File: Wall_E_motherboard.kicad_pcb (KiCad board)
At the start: 4 copper layers, 81.1 x 71.4 mm, 69 parts, among them J1 Conn_01x02, J8 Conn_01x06_Socket, J9 Conn_01x02_Socket, Q1 PMOS, SW1 SW_SPST, SW2 SW_SPST, SW3 SW_SPST, U1 LM1085-ADJ, U2 STM32F411RCTx, U3 DRV8838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

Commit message: Routing Updates
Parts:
- added ArmL1: Conn_01x03_Socket, Connector_PinHeader_2.54mm:PinHeader_1x03_P2.54mm_Vertical, F.Cu at (116.2, 105.9)
- added ArmR1: Conn_01x03_Socket, Connector_PinHeader_2.54mm:PinHeader_1x03_P2.54mm_Vertical, F.Cu at (175.8, 106.1)
- added Camera1: Conn_01x08_Socket, Connector_PinHeader_2.54mm:PinHeader_1x08_P2.54mm_Vertical, F.Cu at (175.8, 67.4)
- added H1: MountingHole, MountingHole:MountingHole_3.2mm_M3, F.Cu at (125.0, 77.2)
- added H2: MountingHole, MountingHole:MountingHole_3.2mm_M3, F.Cu at (175.8, 61.2)
- added H3: MountingHole, MountingHole:MountingHole_3.2mm_M3, F.Cu at (123.2, 123.2)
- added H4: MountingHole, MountingHole:MountingHole_3.2mm_M3, F.Cu at (170.8, 123.5)
- added HandL1: Conn_01x03_Socket, Connector_PinHeader_2.54mm:PinHeader_1x03_P2.54mm_Vertical, F.Cu at (116.2, 114.9)
- added HandR1: Conn_01x03_Socket, Connector_PinHeader_2.54mm:PinHeader_1x03_P2.54mm_Vertical, F.Cu at (175.8, 115.1)
- added LeftMotor1: Conn_01x06_Socket, Connector_PinHeader_2.54mm:PinHeader_1x06_P2.54mm_Vertical, F.Cu at (116.2, 89.2)
- added R16: 10, Resistor_SMD:R_0603_1608Metric, F.Cu at (223.5, 91.4)
- added R17: 10, Resistor_SMD:R_0603_1608Metric, F.Cu at (223.5, 94.2)
- added R18: 10k, Resistor_SMD:R_0603_1608Metric, F.Cu at (157.4, 97.7)
- added R19: 10k, Resistor_SMD:R_0603_1608Metric, F.Cu at (159.0, 98.0)
- added Range1: Conn_01x04_Socket, Connector_PinHeader_2.54mm:PinHeader_1x04_P2.54mm_Vertical, F.Cu at (138.0, 122.0)
- added RightMotor1: Conn_01x06_Socket, Connector_PinHeader_2.54mm:PinHeader_1x06_P2.54mm_Vertical, F.Cu at (175.8, 89.2)
- C11, C9: value 0.1u -> 22u; footprint Capacitor_SMD:C_0603_1608Metric -> Capacitor_THT:CP_Radial_D5.0mm_P2.00mm
- Q1: value PMOS -> SI4435FDY-T1-GE3; footprint Package_TO_SOT_THT:TO-220-3_Vertical -> Wall_E_footprints:SO-8_VIS
- SW3: footprint Button_Switch_THT:SW_PUSH_6mm -> Button_Switch_SMD:SW_SPST_PTS645
- Y1: footprint Crystal:Crystal_SMD_HC49-SD -> Crystal:Crystal_SMD_3225-4Pin_3.2x2.5mm
- Y2, Y3: footprint Crystal:Crystal_SMD_HC49-SD -> Crystal:Crystal_SMD_3215-2Pin_3.2x1.5mm
- moved C12 196.9 mm to (255.3, 73.9)
- moved C13 196.9 mm to (255.3, 76.4)
- moved C14 196.9 mm to (255.3, 78.9)
- moved C15 196.9 mm to (255.3, 81.4)
- moved U4 162.0 mm to (247.2, 73.2)
- moved U5 162.0 mm to (247.2, 76.9)
- moved C25 162.0 mm to (256.8, 97.9)
- moved C9 116.0 mm to (171.0, 97.3), turned to -90 degrees
- moved C8 112.8 mm to (168.0, 96.0), turned to -135 degrees
- moved U3 84.1 mm to (171.5, 94.2), turned to 180 degrees
- moved Y3 72.1 mm to (129.2, 100.2), turned to 180 degrees
- moved C10 71.6 mm to (124.0, 91.8), turned to 45 degrees
- moved C21 63.0 mm to (132.1, 99.9), turned to 90 degrees
- moved C11 61.4 mm to (121.0, 90.5), turned to 90 degrees
- moved R7 60.7 mm to (134.1, 106.0), turned to -90 degrees
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- renumbered J8 to STLink1, J9 to UART1
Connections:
- net Net-(U6-PS0) renamed IMU_PS0
- net Net-(U6-PS1) renamed IMU_PS1
- C11 pad 1: GND -> Vin
- C11 pad 2: Vin -> GND
- C21 pad 2: GND -> Net-(C21-Pad2)
- C22 pad 2: GND -> Net-(C21-Pad2)
- C9 pad 1: GND -> Vin
- C9 pad 2: Vin -> GND
- F1 pad 2: Net-(Q1-D) -> Net-(F1-Pad2)
- Q1 pad 1: Net-(Q1-D) -> Net-(F1-Pad2)
- Q1 pad 2: Net-(Q1-G) -> Net-(F1-Pad2)
- Q1 pad 3: Vin -> Net-(F1-Pad2)
- R9 pad 1: Net-(Q1-G) -> Net-(Q1-Pad4)
- U2 pad 1: 5V -> 3.3V
- U2 pad 14: unconnected-(U2-PA0-Pad14) -> ENCA_left
- U2 pad 15: unconnected-(U2-PA1-Pad15) -> Bat_ADC
- U2 pad 21: unconnected-(U2-PA5-Pad21) -> CAM_SCLK
- U2 pad 22: unconnected-(U2-PA6-Pad22) -> Echo
- U2 pad 23: unconnected-(U2-PA7-Pad23) -> Trig
- U2 pad 26: unconnected-(U2-PB0-Pad26) -> DIR_left
- U2 pad 27: unconnected-(U2-PB1-Pad27) -> DIR_right
- U2 pad 29: unconnected-(U2-PB10-Pad29) -> ENCB_left
- U2 pad 41: unconnected-(U2-PA8-Pad41) -> R_Arm_PWM
- U2 pad 42: unconnected-(U2-PA9-Pad42) -> L_Arm_PWM
- U2 pad 43: unconnected-(U2-PA10-Pad43) -> R_Hand_PWM
- U2 pad 44: unconnected-(U2-PA11-Pad44) -> L_Hand_PWM
- U2 pad 53: unconnected-(U2-PC12-Pad53) -> CAM_CS
- U2 pad 56: unconnected-(U2-PB4-Pad56) -> CAM_MISO
- U2 pad 57: unconnected-(U2-PB5-Pad57) -> CAM_MOSI
- U2 pad 58: unconnected-(U2-PB6-Pad58) -> I2C_SCL
- U2 pad 59: unconnected-(U2-PB7-Pad59) -> ENCA_right
- U2 pad 61: unconnected-(U2-PB8-Pad61) -> ENCB_right
- U2 pad 62: unconnected-(U2-PB9-Pad62) -> I2C_SDA
- U3 pad 6: PH_right -> DIR_right
- U6 pad 10: unconnected-(U6-BL_IND-Pad10) -> GND
- U6 pad 11: unconnected-(U6-~{RESET}-Pad11) -> IMU_NRST
- U6 pad 14: unconnected-(U6-INT-Pad14) -> IMU_INT
- U6 pad 18: unconnected-(U6-COM2-Pad18) -> GND
- U6 pad 19: unconnected-(U6-COM1-Pad19) -> I2C_SCL
- U6 pad 20: unconnected-(U6-COM0-Pad20) -> I2C_SDA
- U6 pad 4: unconnected-(U6-~{BOOT_LOAD_PIN}-Pad4) -> 3.3V
- U7 pad 6: PH_left -> DIR_left
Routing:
- net Vin: track 17.9 -> 98.7 mm, vias 0 -> 4
- net 5V: track 54.5 -> 1.21 mm, vias 2 -> 1
- net CAM_SCLK: track 0.00 -> 46.6 mm, vias 0 -> 2
- net I2C_SCL: track 0.00 -> 45.2 mm
- net I2C_SDA: track 0.00 -> 41.4 mm
- net LED: track 12.8 -> 50.6 mm
- net CAM_MISO: track 0.00 -> 33.6 mm
- net CAM_MOSI: track 0.00 -> 29.5 mm
- net ENCB_right: track 0.00 -> 29.2 mm
- net ENCA_right: track 0.00 -> 28.7 mm
- net CAM_CS: track 0.00 -> 27.2 mm
- net PC15: track 23.7 -> 6.47 mm
- net Net-(F1-Pad2): track 0.00 -> 14.0 mm
- net ST_SWO: track 34.3 -> 21.8 mm
- net PH1: track 20.2 -> 8.09 mm
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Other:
- board size 81.1 x 71.4 mm -> 69.4 x 71.4 mm
- board text added: "Battery"
- board text added: "E-Stop"
- board text added: "On SW"

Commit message: continued routing
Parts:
- removed C12, C13, C14, C15: 0.1u, Capacitor_SMD:C_0603_1608Metric
- removed R16, R17: 10, Resistor_SMD:R_0603_1608Metric
- removed U4, U5: DRV8838, Package_SON:WSON-8-1EP_2x2mm_P0.5mm_EP0.9x1.6mm
- added TP1: TestPoint_Small, TestPoint:TestPoint_Pad_D1.0mm, F.Cu at (122.7, 99.6)
- added TP2: TestPoint_Small, TestPoint:TestPoint_Pad_D1.0mm, F.Cu at (188.0, 102.0)
- moved C25 102.7 mm to (154.1, 95.6), turned to 90 degrees
- moved R7 4.17 mm to (138.1, 107.2), turned to 0 degrees
- moved STLink1 4.04 mm to (162.6, 119.1)
- moved UART1 4.04 mm to (146.1, 119.1)
- moved H4 3.91 mm to (169.0, 120.0)
- moved H3 3.69 mm to (125.0, 120.0)
- moved C21 3.51 mm to (135.3, 101.2)
- moved C22 3.51 mm to (129.6, 101.2)
- moved U6 3.51 mm to (133.5, 106.0)
- moved Y3 3.51 mm to (132.5, 101.5)
- moved C19 3.51 mm to (132.0, 109.1)
- moved R5 3.51 mm to (129.6, 109.1)
- moved C24 3.51 mm to (128.9, 105.3)
- moved C20 3.51 mm to (128.9, 103.6)
- moved R6 3.51 mm to (128.9, 106.8)
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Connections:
- U2 pad 25: unconnected-(U2-PC5-Pad25) -> SL_left
- U2 pad 28: unconnected-(U2-PB2-Pad28) -> SL_right
- U2 pad 41: R_Arm_PWM -> L_Arm_PWM
- U2 pad 42: L_Arm_PWM -> L_Hand_PWM
- U2 pad 44: L_Hand_PWM -> R_Arm_PWM
- U2 pad 50: unconnected-(U2-PA15-Pad50) -> EN_right
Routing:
- net 5V: track 1.21 -> 124.8 mm, vias 1 -> 9
- net Vin: track 98.7 -> 190.1 mm, vias 4 -> 8
- net L_Hand_PWM: track 0.00 -> 52.4 mm
- net L_Arm_PWM: track 0.00 -> 49.6 mm
- net ENCB_left: track 0.00 -> 43.1 mm
- net DIR_left: track 0.00 -> 42.4 mm
- net SL_left: track 0.00 -> 41.5 mm
- net ENCA_left: track 0.00 -> 33.5 mm, vias 0 -> 1
- net DIR_right: track 0.00 -> 29.4 mm
- net SL_right: track 0.00 -> 28.9 mm
- net R_Hand_PWM: track 0.00 -> 25.8 mm
- net Bat_ADC: track 1.61 -> 27.4 mm, vias 0 -> 2
- net I2C_SDA: track 41.4 -> 63.9 mm
- net I2C_SCL: track 45.2 -> 67.6 mm
- net R_Arm_PWM: track 0.00 -> 18.7 mm
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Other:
- board size 69.4 x 71.4 mm -> 69.4 x 67.8 mm

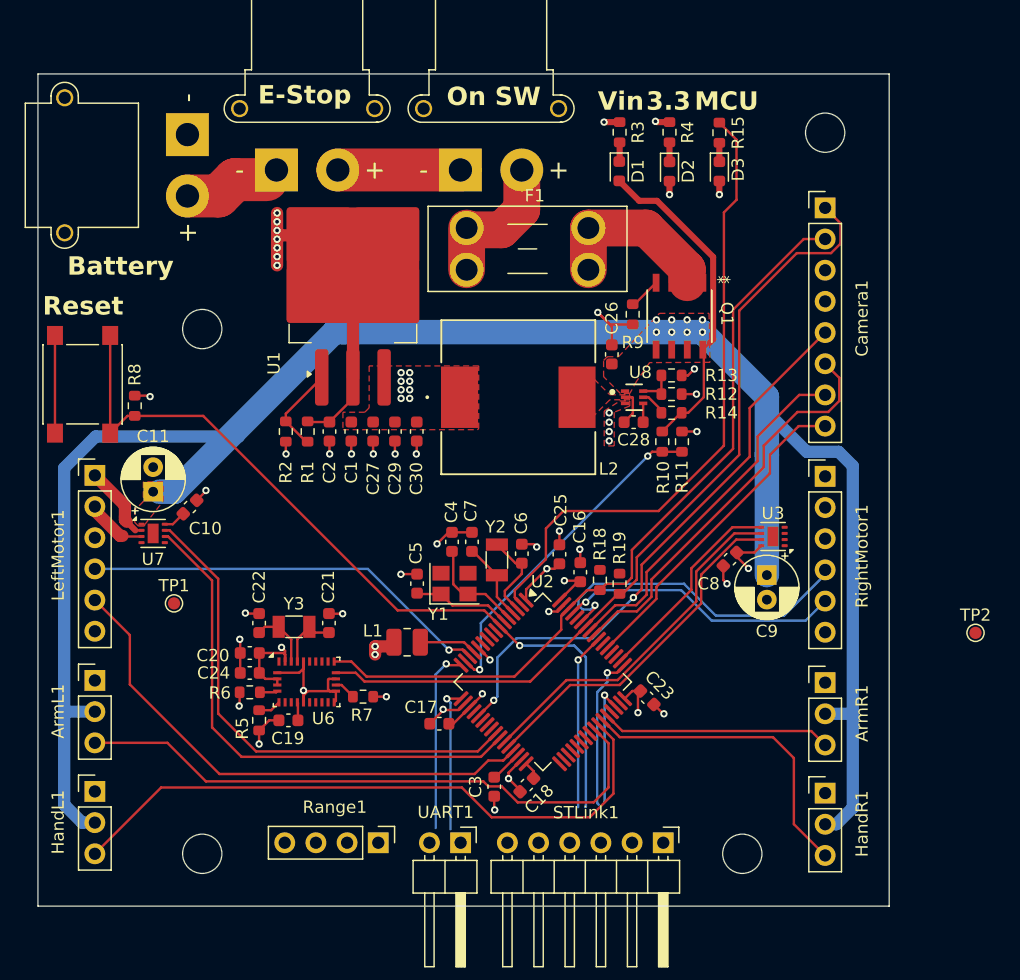
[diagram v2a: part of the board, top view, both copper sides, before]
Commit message: Routing first draft complete
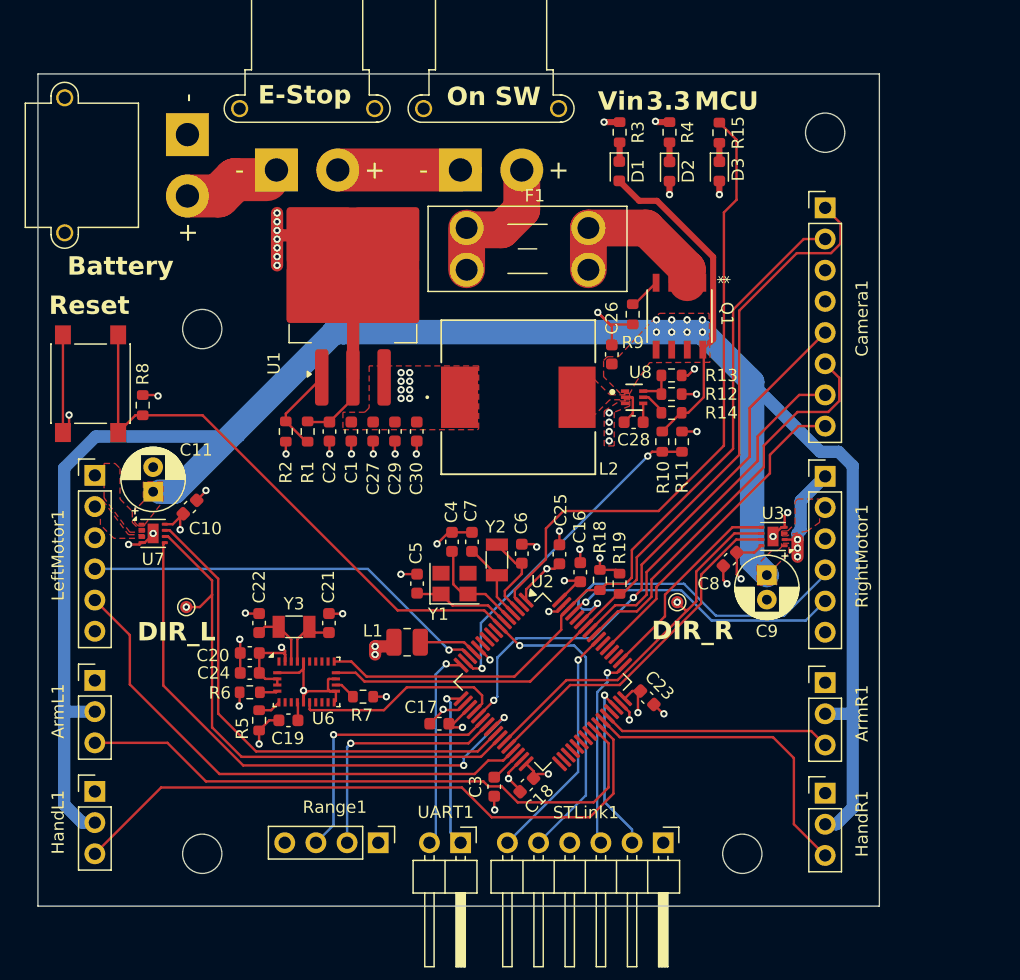
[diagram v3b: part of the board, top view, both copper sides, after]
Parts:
- moved TP2 24.4 mm to (163.7, 99.5)
- moved TP1 1.04 mm to (123.7, 99.9)
- moved R8 0.65 mm to (120.2, 83.5)
- moved SW3 0.65 mm to (115.9, 81.7)
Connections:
- net IMU_PS0 renamed Net-(U6-PS0)
- net IMU_PS1 renamed Net-(U6-PS1)
- C21 pad 2: Net-(C21-Pad2) -> GND
- C22 pad 2: Net-(C21-Pad2) -> GND
- U2 pad 20: unconnected-(U2-PA4-Pad20) -> IMU_NRST
- U2 pad 24: unconnected-(U2-PC4-Pad24) -> EN_left
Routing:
- net EN_left: track 0.00 -> 45.6 mm, vias 0 -> 2
- net Echo: track 0.00 -> 22.0 mm, vias 0 -> 1
- net Trig: track 0.00 -> 20.0 mm, vias 0 -> 1
- net IMU_NRST: track 0.00 -> 17.3 mm
- net GND: track 70.0 -> 80.6 mm, vias 35 -> 41
- net M1_right: track 0.00 -> 8.53 mm, vias 0 -> 3
- net M1_left: track 6.48 -> 0.00 mm
- net 3.3V: track 59.8 -> 65.5 mm, vias 18 -> 21
- net ST_SWO: track 14.4 -> 19.7 mm
- net M2_left: track 5.35 -> 0.68 mm
- net ST_SWDIO: track 10.1 -> 14.3 mm
- net NRST: track 67.7 -> 71.5 mm
- net ST_SWCLK: track 12.8 -> 16.0 mm
- net DIR_left: track 42.4 -> 44.9 mm, vias 0 -> 1
- net Net-(C21-Pad2): track 2.26 -> 0.00 mm
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- added copper zone on F.Cu, net M1_left
- added copper zone on F.Cu, net M2_left
- added copper zone on F.Cu, net M2_right
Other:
- board size 69.4 x 67.8 mm -> 68.6 x 67.8 mm
- board text added: "DIR_L"
- board text added: "DIR_R"

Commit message: Final commit before Charlie review
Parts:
- added TP3: TestPoint_Small, TestPoint:TestPoint_Pad_D1.0mm, F.Cu at (160.2, 90.6)
- C2, C27, C29: footprint Capacitor_SMD:C_0603_1608Metric -> Capacitor_THT:CP_Radial_D5.0mm_P2.00mm
- R1: value R -> 16.5k 1%
- R2: value R -> 10k 1%
- moved C2 14.7 mm to (129.8, 72.0), turned to 180 degrees
- moved R1 7.79 mm to (130.6, 78.4)
- moved C27 7.32 mm to (131.6, 85.6)
- moved R2 5.01 mm to (129.8, 81.0), turned to 180 degrees
- moved C1 3.66 mm to (140.8, 85.6)
- moved C29 3.50 mm to (137.2, 85.6)
- moved R8 1.33 mm to (121.5, 83.2)
- moved SW3 1.33 mm to (117.2, 81.4)
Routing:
- net 5V: track 124.8 -> 132.4 mm, vias 9 -> 1
- net /Power Regulation/buck_sw: track 2.93 -> 9.04 mm, vias 0 -> 1
- net GND: track 80.6 -> 77.4 mm, vias 41 -> 38
- net Net-(U1-ADJ): track 7.24 -> 6.00 mm
- net NRST: track 71.5 -> 70.3 mm
- net 3.3V: track 65.5 -> 65.9 mm, vias 21 -> 14
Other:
- board size 68.6 x 67.8 mm -> 68 x 68 mm
- board text added: "SW"

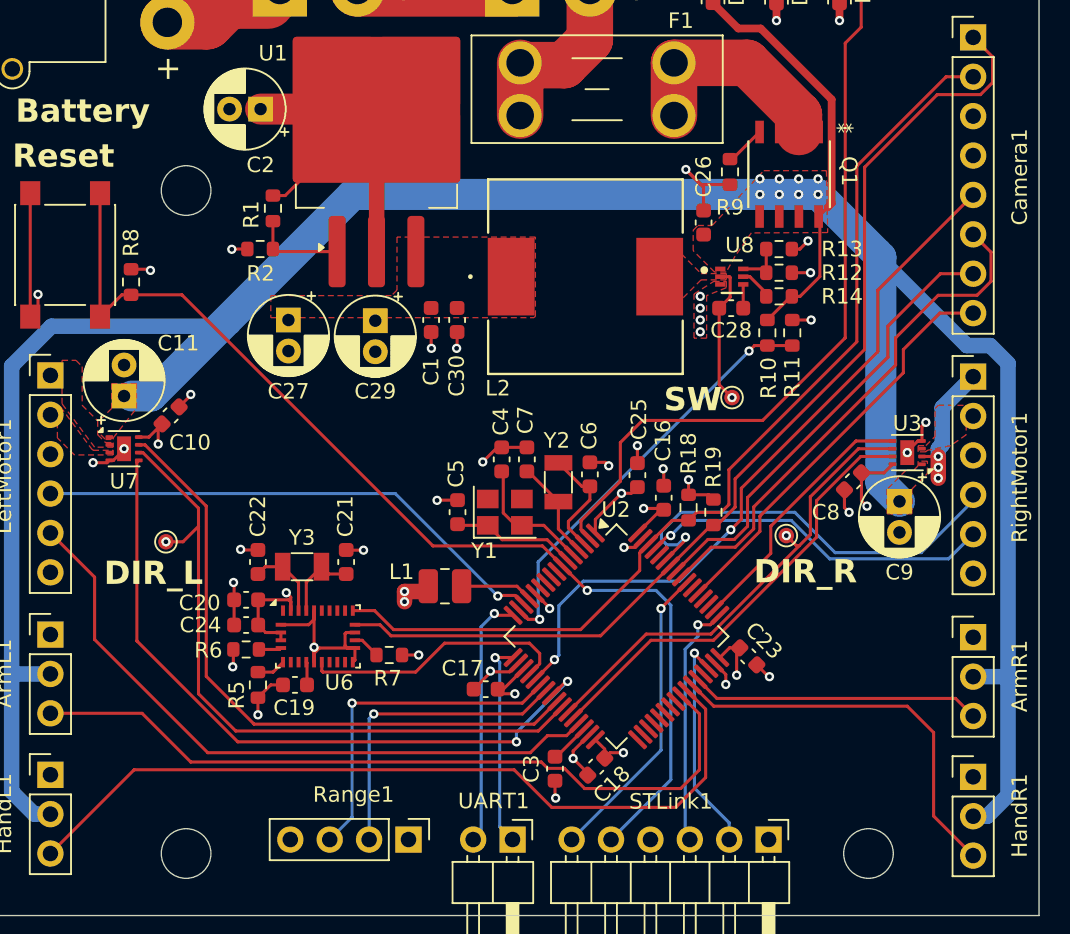
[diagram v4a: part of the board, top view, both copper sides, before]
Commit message: added resistor divider to Echo pin
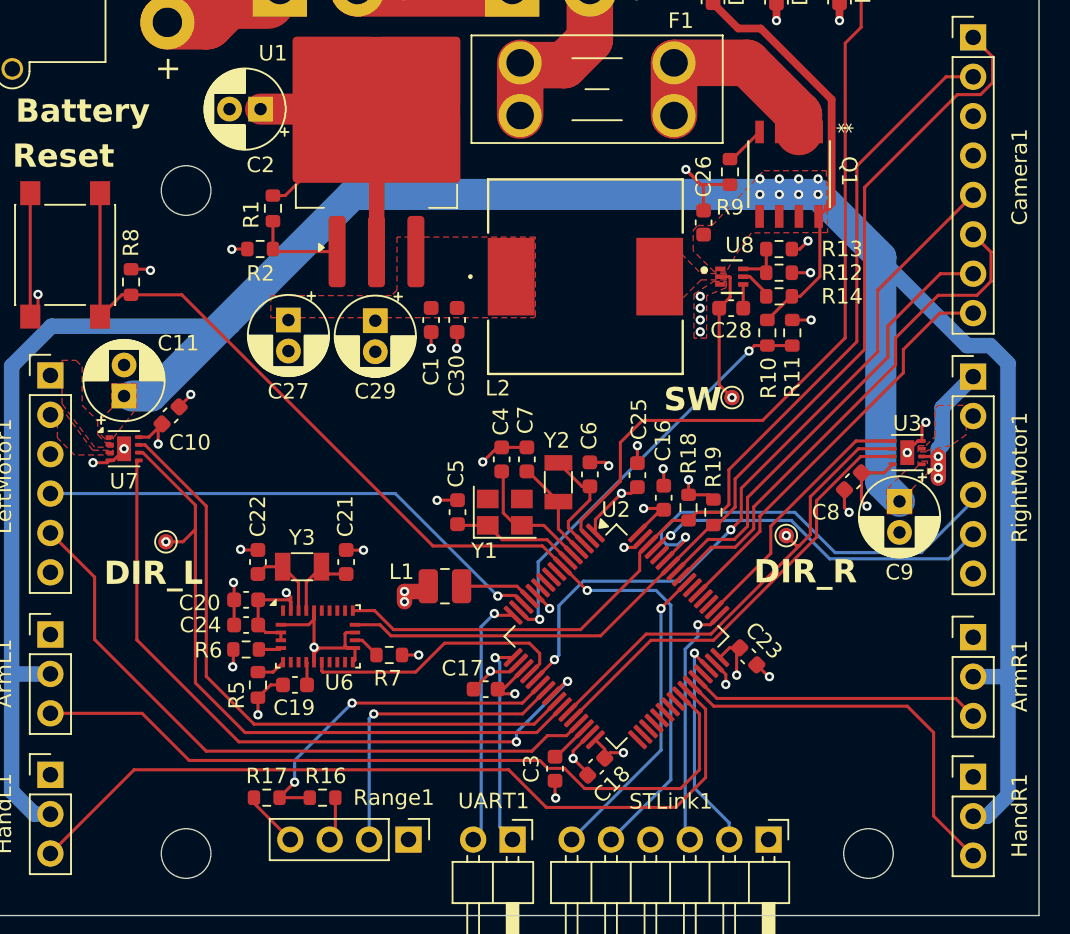
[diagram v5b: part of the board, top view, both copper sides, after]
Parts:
- added R16: 5k, Resistor_SMD:R_0603_1608Metric, F.Cu at (133.8, 116.4)
- added R17: 10k, Resistor_SMD:R_0603_1608Metric, F.Cu at (130.2, 116.4)
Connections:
- Range1 pad 3: Echo -> Net-(Range1-Pin_3)
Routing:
- net GND: track 77.4 -> 81.1 mm
- net Net-(Range1-Pin_3): track 0.00 -> 2.85 mm
- net I2C_SCL: track 67.6 -> 66.8 mm
- net Echo: track 22.0 -> 22.6 mm, vias 1 -> 2

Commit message: Final design before order
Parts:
- added C12: 0.1u, Capacitor_SMD:C_0603_1608Metric, F.Cu at (145.0, 99.8)
- added C13: 0.1u, Capacitor_SMD:C_0603_1608Metric, F.Cu at (145.0, 101.4)
- added R20: 10k, Resistor_SMD:R_0603_1608Metric, F.Cu at (160.0, 92.2)
- C3: value 2.2u -> 4.7u
- R18, R19: value 10k -> 2.2k
- R3: value 500 -> 60
- moved R9 7.33 mm to (167.4, 76.2), turned to 90 degrees
- moved TP3 2.95 mm to (158.8, 88.0)
- moved Q1 2.02 mm to (163.6, 74.2), turned to 90 degrees
- moved TP1 1.90 mm to (123.6, 98.0)
- moved C4 1.80 mm to (146.2, 93.0)
- moved C7 1.79 mm to (147.8, 93.0)
- moved C23 1.78 mm to (163.0, 107.0), turned to 0 degrees
- moved Y1 1.65 mm to (146.0, 96.4), turned to 180 degrees
- moved C5 1.59 mm to (142.6, 96.4)
- moved Y2 1.49 mm to (149.8, 94.8)
- moved C6 1.49 mm to (151.8, 94.3)
- moved L1 0.94 mm to (141.0, 103.4)
- moved C20 0.87 mm to (128.0, 103.6)
- moved C24 0.87 mm to (128.0, 105.2)
- moved R5 0.87 mm to (128.8, 109.1)
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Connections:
- Q1 pad 1: Net-(F1-Pad2) -> Vin
- Q1 pad 2: Net-(F1-Pad2) -> Vin
- Q1 pad 3: Net-(F1-Pad2) -> Vin
- Q1 pad 5: Vin -> Net-(F1-Pad2)
- Q1 pad 6: Vin -> Net-(F1-Pad2)
- Q1 pad 7: Vin -> Net-(F1-Pad2)
- Q1 pad 8: Vin -> Net-(F1-Pad2)
- U2 pad 60: unconnected-(U2-BOOT0-Pad60) -> Net-(U2-BOOT0)
- Y1 pad 1: PH1 -> PH0
- Y1 pad 2: PH0 -> GND
- Y1 pad 3: (no net) -> PH1
- Y1 pad 4: (no net) -> GND
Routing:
- net Vin: track 191.5 -> 39.3 mm, vias 8 -> 12
- net Net-(F1-Pad2): track 14.0 -> 0.00 mm
- net Net-(U2-BOOT0): track 0.00 -> 13.9 mm, vias 0 -> 2
- net GND: track 81.1 -> 87.8 mm, vias 38 -> 42
- net /Power Regulation/buck_sw: track 9.04 -> 6.33 mm
- net Net-(U2-VDDA): track 4.72 -> 7.19 mm
- net PC15: track 6.47 -> 8.33 mm
- net PC14: track 7.38 -> 8.97 mm
- net L_Hand_PWM: track 52.4 -> 54.0 mm
- net NRST: track 70.3 -> 71.8 mm
- net L_Arm_PWM: track 49.6 -> 50.8 mm
- net DIR_left: track 44.4 -> 45.5 mm
- net Net-(U6-CAP): track 1.48 -> 2.35 mm
- net Net-(U6-PS1): track 1.46 -> 2.30 mm
- net Net-(U6-PS0): track 1.88 -> 2.73 mm
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- added copper zone on F.Cu, net Net-(F1-Pad2)
- added copper zone on B.Cu, net Vin
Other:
- board size 68 x 68 mm -> 69 x 69 mm
